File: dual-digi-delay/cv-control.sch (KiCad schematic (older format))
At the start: 44 parts, among them Q3 2N3904, Q4 2N3904, Q5 2N3904, Q6 2N3904, U5 TL074, U6 TL074

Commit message: Final revision of dual digi delay
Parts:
- added C56: 10pF, rumblesan-footprints:C_Rect_L7.0mm_W3.5mm_P5.00mm, symbol Device:C
- added D13, D14, D15, D16: 1n4148, rumblesan-footprints:Diode_THT_P7.62mm_Horizontal, symbol Device:D
- added R64, R66: 10k, rumblesan-footprints:Resistor_THT_L6.3mm_D2.5mm_P10.16mm_Horizontal, symbol Device:R
- added R65, R67: 1k, rumblesan-footprints:Resistor_THT_L6.3mm_D2.5mm_P10.16mm_Horizontal, symbol Device:R
- added R68, R69: 47k, rumblesan-footprints:Resistor_THT_L6.3mm_D2.5mm_P10.16mm_Horizontal, symbol Device:R
- R35: value 47k -> 100k
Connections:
- net DELAY1_CONTROL: now also R37.1; no longer R37.2
- net DELAY1_CV_ATTV: now also U6.3 (+), R69.1; no longer U6.5 (+)
- net DELAY2_CONTROL: now also R43.1; no longer R43.2
- net DELAY2_CV_ATTV: now also U6.12 (+), R68.1; no longer U5.3 (+)
- net DELAY2_CV_CTRL: now also U6.8, C56.1, R66.1, R68.2; no longer U5.7
- net GND: now also U5.3 (+), U6.5 (+), R65.1, R67.1; no longer U6.12 (+), U6.3 (+)
- net at R31.2, R32.2, R33.1: now also U6.9 (-), C56.2, D15.1 (K), D16.2 (A); no longer U5.6 (-)
- net at C45.2, R51.2: now also U5.14; no longer U5.8
- net at C45.1, Q3.3 (C), R50.2: now also U5.13 (-); no longer U5.9 (-)
- net at C43.2, R42.1, R44.1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: now also U5.9 (-); no longer R43.1, U5.13 (-)
- net at C43.1, R48.1: now also U5.8; no longer U5.14
- net at C41.1, R40.1, R42.2: now also U6.14; no longer U5.1
- net at C41.2, R36.1, R40.2: now also R43.2, U6.13 (-); no longer U5.2 (-)
- net at C40.2, R30.1, R34.2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: now also D13.1 (K), D14.2 (A)
- net DELAY1_CV_CTRL: now reaches C40.1, R34.1, R35.2, U6.7
- net DELAY1_CV_CTRL: now also R64.1, R69.2
- net at C46.2, R53.2: now also U5.1; no longer U6.8
- net at C46.1, Q4.3 (C), R52.2: now also U5.2 (-); no longer U6.9 (-)
- net at C44.2, R45.1, R47.2: now also R39.1, U5.6 (-); no longer U6.13 (-)
- net at C44.1, R49.1: now also U5.7; no longer U6.14
- net at C42.2, R35.1, R41.2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: now also R37.2; no longer R37.1, R39.1
- new net: D13.2 (A), D14.1 (K), R64.2, R65.2
- new net: D15.2 (A), D16.1 (K), R66.2, R67.2
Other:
- note added: "POT CW\nPIN 3"
- moved on the sheet: C36, C37, C38, C39, C40, C41, C43, C45, Q3, Q5, R29, R30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

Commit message: Finalising rev 01 of dual digi delay
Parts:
- R37, R43: value 100k -> 220k
- R42: value 47k -> 100k
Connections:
- net +VCC: no longer R39.2, R44.2
- net -VCC: now also R39.2, R44.2
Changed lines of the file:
@@
 $Descr A4 11693 8268
 encoding utf-8
-Sheet 10 10
+Sheet 9 10
 Title ""
 Date ""
@@
 AR Path="/642384B2/642A547E" Ref="R42"  Part="1"
 F 0 "R42" V 6443 5150 50  0000 C CNN
-F 1 "47k" V 6534 5150 50  0000 C CNN
+F 1 "100k" V 6534 5150 50  0000 C CNN
 F 2 "rumblesan-footprints:Resistor_THT_L6.3mm_D2.5mm_P10.16mm_Horizontal" V 6580 5150 50  0001 C CNN
 F 3 "~" H 6650 5150 50  0001 C CNN
@@
 AR Path="/642A54A8" Ref="U?"  Part="1"
 AR Path="/642384B2/642A54A8" Ref="U5"  Part="1"
-F 0 "U5" H 9000 2533 50  0000 C CNN
-F 1 "TL074" H 9000 2624 50  0000 C CNN
+F 0 "U5" H 9000 3200 50  0000 C CNN
+F 1 "TL074" H 9000 3100 50  0000 C CNN
 F 2 "rumblesan-footprints:DIP-14_W7.62mm_Socket" H 8950 3000 50  0001 C CNN
 F 3 "http://www.ti.com/lit/ds/symlink/tl071.pdf" H 9050 3100 50  0001 C CNN
@@
 AR Path="/642384B2/642A55A5" Ref="R43"  Part="1"
 F 0 "R43" V 5093 4200 50  0000 C CNN
-F 1 "100k" V 5184 4200 50  0000 C CNN
+F 1 "220k" V 5184 4200 50  0000 C CNN
 F 2 "rumblesan-footprints:Resistor_THT_L6.3mm_D2.5mm_P10.16mm_Horizontal" V 5230 4200 50  0001 C CNN
 F 3 "~" H 5300 4200 50  0001 C CNN
@@
 AR Path="/642384B2/642A55EA" Ref="R37"  Part="1"
 F 0 "R37" V 5093 1150 50  0000 C CNN
-F 1 "100k" V 5184 1150 50  0000 C CNN
+F 1 "220k" V 5184 1150 50  0000 C CNN
 F 2 "rumblesan-footprints:Resistor_THT_L6.3mm_D2.5mm_P10.16mm_Horizontal" V 5230 1150 50  0001 C CNN
 F 3 "~" H 5300 1150 50  0001 C CNN
@@
 Text Label 7250 2350 2    50   ~ 0
 GND1
-Text Label 6450 900  2    50   ~ 0
-+VCC
 Text Label 4700 3150 3    50   ~ 0
 GND1
@@
 Text Label 8800 6000 2    50   ~ 0
 GND1
-Text Label 6650 4050 2    50   ~ 0
-+VCC
 Text Label 9450 3850 2    50   ~ 0
 +VCC
@@
 	1    0    0    1
 $EndComp
+Text Label 6450 900  2    50   ~ 0
+-VCC
+Text Label 6650 4050 2    50   ~ 0
+-VCC
 $EndSCHEMATC

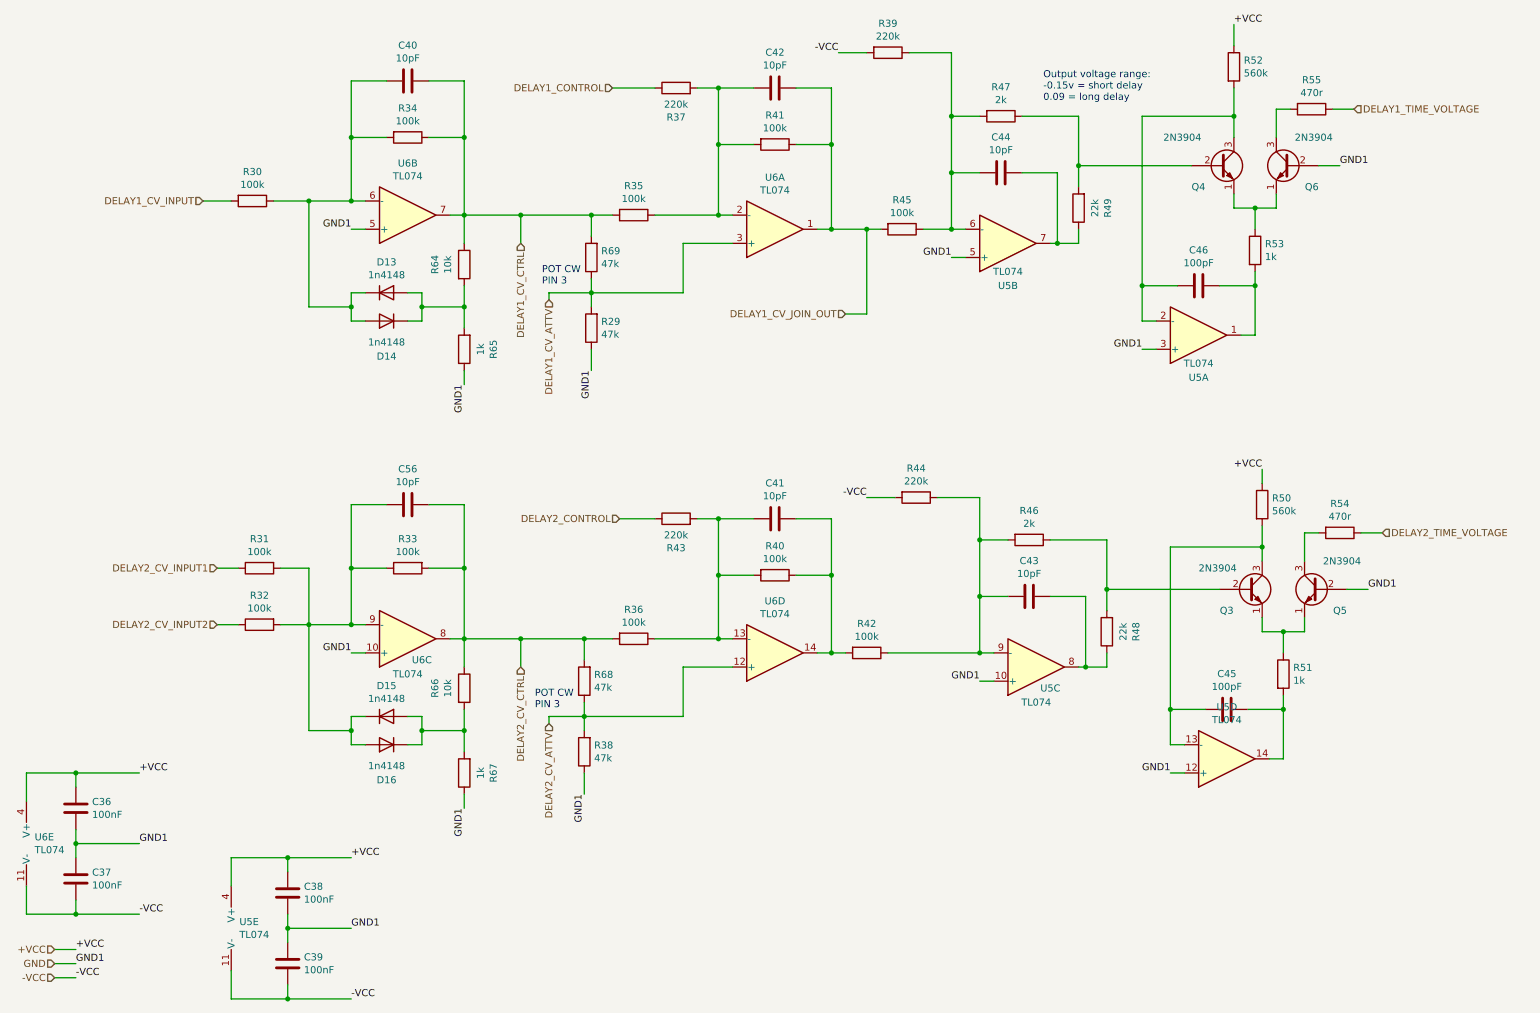
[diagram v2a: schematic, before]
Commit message: Updating digi delay to rev 2
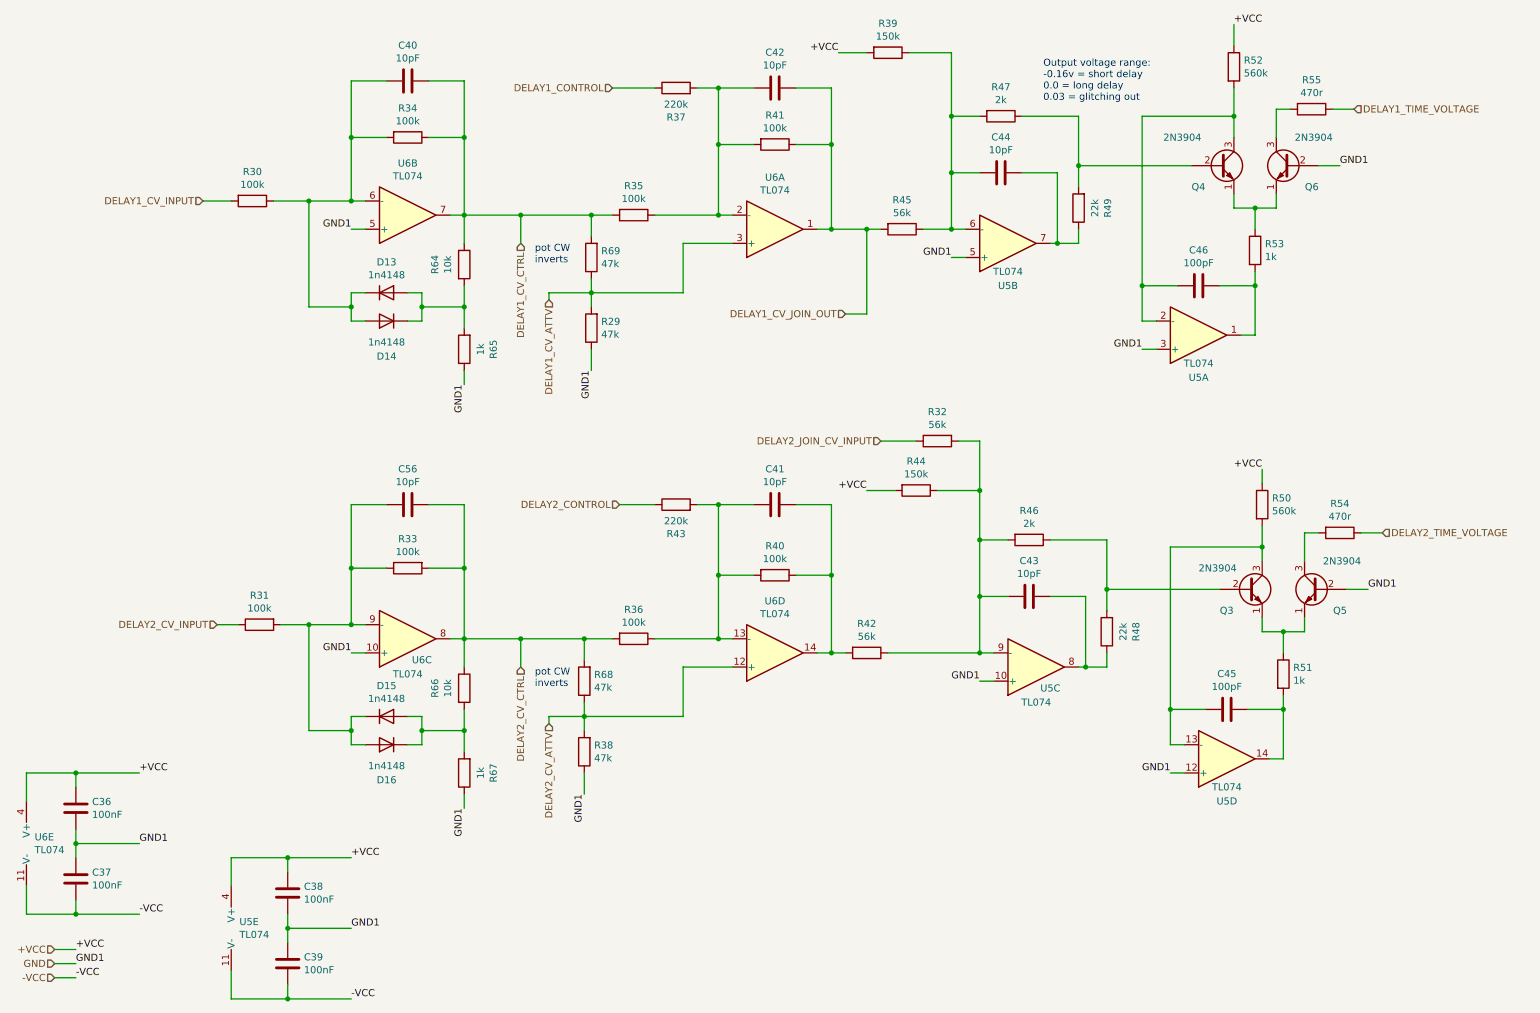
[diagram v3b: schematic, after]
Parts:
- Q3, Q4, Q5, Q6: footprint Package_TO_SOT_THT:TO-92_Inline -> Package_TO_SOT_THT:TO-92_Inline_Wide
- R32, R42, R45: value 100k -> 56k
- R39, R44: value 220k -> 150k
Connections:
- net +VCC: now also R39.2, R44.2
- net -VCC: no longer R39.2, R44.2
- net at C43.2, R42.1, R44.1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: now also R32.2
- net at C56.2, D15.1 (K), D16.2 (A)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: no longer R32.2
- net DELAY2_CV_INPUT1 renamed DELAY2_CV_INPUT
- net DELAY2_CV_INPUT2 renamed DELAY2_JOIN_CV_INPUT
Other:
- note added: "Output voltage range:\n-0.16v = short delay\n0.0 = long delay\n0.03 = glitching out"
- note added: "pot CW\ninverts"
- note removed: "Output voltage range:\n-0.15v = short delay\n0.09 = long delay"
- note removed: "POT CW\nPIN 3"
- moved on the sheet: C41, R31, R32, R43, R44
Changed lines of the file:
@@
 $Descr A4 11693 8268
 encoding utf-8
-Sheet 9 10
+Sheet 8 11
 Title ""
 Date ""
@@
 L Device:R R?
 U 1 1 642A5416
-P 7000 4050
+P 7000 4000
 AR Path="/642A5416" Ref="R?"  Part="1"
 AR Path="/642384B2/642A5416" Ref="R44"  Part="1"
-F 0 "R44" V 6793 4050 50  0000 C CNN
-F 1 "220k" V 6884 4050 50  0000 C CNN
-F 2 "rumblesan-footprints:Resistor_THT_L6.3mm_D2.5mm_P10.16mm_Horizontal" V 6930 4050 50  0001 C CNN
-F 3 "~" H 7000 4050 50  0001 C CNN
-	1    7000 4050
-	0    1    1    0
-$EndComp
-Wire Wire Line
-	7150 4050 7450 4050
-Wire Wire Line
-	6650 4050 6850 4050
+F 0 "R44" V 6793 4000 50  0000 C CNN
+F 1 "150k" V 6884 4000 50  0000 C CNN
+F 2 "rumblesan-footprints:Resistor_THT_L6.3mm_D2.5mm_P10.16mm_Horizontal" V 6930 4000 50  0001 C CNN
+F 3 "~" H 7000 4000 50  0001 C CNN
+	1    7000 4000
+	0    1    1    0
+$EndComp
+Wire Wire Line
+	7150 4000 7450 4000
+Wire Wire Line
+	6650 4000 6850 4000
 Wire Wire Line
 	7450 5150 7450 4750
@@
 	7650 4750 7450 4750
 Connection ~ 7450 4750
-Wire Wire Line
-	7450 4750 7450 4350
 Wire Wire Line
 	7950 4350 8350 4350
@@
 F 0 "Q5" H 9650 4550 50  0000 L CNN
 F 1 "2N3904" H 9550 4900 50  0000 L CNN
-F 2 "Package_TO_SOT_THT:TO-92_Inline" H 10050 4625 50  0001 L CIN
+F 2 "Package_TO_SOT_THT:TO-92_Inline_Wide" H 10050 4625 50  0001 L CIN
 F 3 "https://www.onsemi.com/pub/Collateral/2N3903-D.PDF" H 9850 4700 50  0001 L CNN
 	1    9850 4700
@@
 Connection ~ 5600 4600
 Wire Wire Line
-	5850 4200 5600 4200
+	5850 4100 5600 4100
 Connection ~ 6400 4600
 Wire Wire Line
-	6400 4200 6150 4200
-Wire Wire Line
-	6400 4600 6400 4200
+	6400 4100 6150 4100
 Wire Wire Line
 	6400 5150 6500 5150
@@
 AR Path="/642384B2/642A547E" Ref="R42"  Part="1"
 F 0 "R42" V 6443 5150 50  0000 C CNN
-F 1 "100k" V 6534 5150 50  0000 C CNN
+F 1 "56k" V 6534 5150 50  0000 C CNN
 F 2 "rumblesan-footprints:Resistor_THT_L6.3mm_D2.5mm_P10.16mm_Horizontal" V 6580 5150 50  0001 C CNN
 F 3 "~" H 6650 5150 50  0001 C CNN
@@
 L Device:C C?
 U 1 1 642A5484
-P 6000 4200
+P 6000 4100
 AR Path="/642A5484" Ref="C?"  Part="1"
 AR Path="/642384B2/642A5484" Ref="C41"  Part="1"
-F 0 "C41" V 5748 4200 50  0000 C CNN
-F 1 "10pF" V 5839 4200 50  0000 C CNN
-F 2 "rumblesan-footprints:C_Rect_L7.0mm_W3.5mm_P5.00mm" H 6038 4050 50  0001 C CNN
-F 3 "~" H 6000 4200 50  0001 C CNN
-	1    6000 4200
+F 0 "C41" V 5748 4100 50  0000 C CNN
+F 1 "10pF" V 5839 4100 50  0000 C CNN
+F 2 "rumblesan-footprints:C_Rect_L7.0mm_W3.5mm_P5.00mm" H 6038 3950 50  0001 C CNN
+F 3 "~" H 6000 4100 50  0001 C CNN
+	1    6000 4100
 	0    1    1    0
 $EndComp
@@
 F 0 "Q6" H 9450 1550 50  0000 L CNN
 F 1 "2N3904" H 9350 1900 50  0000 L CNN
-F 2 "Package_TO_SOT_THT:TO-92_Inline" H 9850 1625 50  0001 L CIN
+F 2 "Package_TO_SOT_THT:TO-92_Inline_Wide" H 9850 1625 50  0001 L CIN
 F 3 "https://www.onsemi.com/pub/Collateral/2N3903-D.PDF" H 9650 1700 50  0001 L CNN
 	1    9650 1700
@@
 F 0 "Q4" H 8950 1550 50  0000 L CNN
 F 1 "2N3904" H 8750 1900 50  0000 L CNN
-F 2 "Package_TO_SOT_THT:TO-92_Inline" H 9350 1625 50  0001 L CIN
+F 2 "Package_TO_SOT_THT:TO-92_Inline_Wide" H 9350 1625 50  0001 L CIN
 F 3 "https://www.onsemi.com/pub/Collateral/2N3903-D.PDF" H 9150 1700 50  0001 L CNN
 	1    9150 1700
@@
 AR Path="/642384B2/642A558B" Ref="R45"  Part="1"
 F 0 "R45" V 6693 2150 50  0000 C CNN
-F 1 "100k" V 6784 2150 50  0000 C CNN
+F 1 "56k" V 6784 2150 50  0000 C CNN
 F 2 "rumblesan-footprints:Resistor_THT_L6.3mm_D2.5mm_P10.16mm_Horizontal" V 6830 2150 50  0001 C CNN
 F 3 "~" H 6900 2150 50  0001 C CNN
@@
 L Device:R R?
 U 1 1 642A55A5
-P 5300 4200
+P 5300 4100
 AR Path="/642A55A5" Ref="R?"  Part="1"
 AR Path="/642384B2/642A55A5" Ref="R43"  Part="1"
-F 0 "R43" V 5093 4200 50  0000 C CNN
-F 1 "220k" V 5184 4200 50  0000 C CNN
-F 2 "rumblesan-footprints:Resistor_THT_L6.3mm_D2.5mm_P10.16mm_Horizontal" V 5230 4200 50  0001 C CNN
-F 3 "~" H 5300 4200 50  0001 C CNN
-	1    5300 4200
+F 0 "R43" V 5093 4100 50  0000 C CNN
+F 1 "220k" V 5184 4100 50  0000 C CNN
+F 2 "rumblesan-footprints:Resistor_THT_L6.3mm_D2.5mm_P10.16mm_Horizontal" V 5230 4100 50  0001 C CNN
+F 3 "~" H 5300 4100 50  0001 C CNN
+	1    5300 4100
 	0    -1   -1   0
 $EndComp
 Text Notes 7900 1250 0    50   ~ 0
-Output voltage range:\n-0.15v = short delay\n0.09 = long delay
+Output voltage range:\n-0.16v = short delay\n0.0 = long delay\n0.03 = glitching out
 Wire Wire Line
 	7050 2150 7250 2150
@@
 L Device:R R?
 U 1 1 642A55BC
-P 2350 4550
+P 2350 4950
 AR Path="/642A55BC" Ref="R?"  Part="1"
 AR Path="/642384B2/642A55BC" Ref="R31"  Part="1"
-F 0 "R31" V 2143 4550 50  0000 C CNN
-F 1 "100k" V 2234 4550 50  0000 C CNN
-F 2 "rumblesan-footprints:Resistor_THT_L6.3mm_D2.5mm_P10.16mm_Horizontal" V 2280 4550 50  0001 C CNN
-F 3 "~" H 2350 4550 50  0001 C CNN
-	1    2350 4550
-	0    -1   1    0
-$EndComp
-Wire Wire Line
-	2050 4550 2200 4550
-Wire Wire Line
-	3000 4950 3000 4550
-Wire Wire Line
-	3000 4550 3250 4550
-Wire Wire Line
-	3000 4950 3100 4950
-Wire Wire Line
-	3700 5050 3800 5050
-Wire Wire Line
-	3550 4550 3800 4550
-Wire Wire Line
-	3800 4550 3800 5050
-Connection ~ 3800 5050
-$Comp
-L Device:R R?
-U 1 1 642A55CC
-P 2350 4950
-AR Path="/642A55CC" Ref="R?"  Part="1"
-AR Path="/642384B2/642A55CC" Ref="R32"  Part="1"
-F 0 "R32" V 2143 4950 50  0000 C CNN
+F 0 "R31" V 2143 4950 50  0000 C CNN
 F 1 "100k" V 2234 4950 50  0000 C CNN
 F 2 "rumblesan-footprints:Resistor_THT_L6.3mm_D2.5mm_P10.16mm_Horizontal" V 2280 4950 50  0001 C CNN
@@
 	0    -1   1    0
 $EndComp
+Wire Wire Line
+	2050 4950 2200 4950
+Wire Wire Line
+	3000 4950 3000 4550
+Wire Wire Line
+	3000 4550 3250 4550
+Wire Wire Line
+	3000 4950 3100 4950
+Wire Wire Line
+	3700 5050 3800 5050
+Wire Wire Line
+	3550 4550 3800 4550
+Wire Wire Line
+	3800 4550 3800 5050
+Connection ~ 3800 5050
 $Comp
 L Device:R R?
@@
 AR Path="/642384B2/642A55DA" Ref="R39"  Part="1"
 F 0 "R39" V 6593 900 50  0000 C CNN
-F 1 "220k" V 6684 900 50  0000 C CNN
+F 1 "150k" V 6684 900 50  0000 C CNN
 F 2 "rumblesan-footprints:Resistor_THT_L6.3mm_D2.5mm_P10.16mm_Horizontal" V 6730 900 50  0001 C CNN
 F 3 "~" H 6800 900 50  0001 C CNN
@@
 	4650 6000 4650 6150
 Wire Wire Line
-	2200 4950 2050 4950
-Wire Wire Line
 	8600 2550 8600 1350
 Wire Wire Line
@@
 F 0 "Q3" H 9150 4550 50  0000 L CNN
 F 1 "2N3904" H 9000 4850 50  0000 L CNN
-F 2 "Package_TO_SOT_THT:TO-92_Inline" H 9550 4625 50  0001 L CIN
+F 2 "Package_TO_SOT_THT:TO-92_Inline_Wide" H 9550 4625 50  0001 L CIN
 F 3 "https://www.onsemi.com/pub/Collateral/2N3903-D.PDF" H 9350 4700 50  0001 L CNN
 	1    9350 4700
@@
 AR Path="/642A55AE" Ref="U?"  Part="4"
 AR Path="/642384B2/642A55AE" Ref="U5"  Part="4"
-F 0 "U5" H 9200 5533 50  0000 C CNN
-F 1 "TL074" H 9200 5624 50  0000 C CNN
+F 0 "U5" H 9200 6200 50  0000 C CNN
+F 1 "TL074" H 9200 6100 50  0000 C CNN
 F 2 "rumblesan-footprints:DIP-14_W7.62mm_Socket" H 9150 6000 50  0001 C CNN
 F 3 "http://www.ti.com/lit/ds/symlink/tl071.pdf" H 9250 6100 50  0001 C CNN
@@
 Text Label 4650 6150 3    50   ~ 0
 GND1
-Text HLabel 4900 4200 0    50   Input ~ 0
+Text HLabel 4900 4100 0    50   Input ~ 0
 DELAY2_CONTROL
 Text Label 7450 5350 2    50   ~ 0
@@
 	1    0    0    -1
 $EndComp
+Text HLabel 6750 3650 0    50   Input ~ 0
+DELAY2_JOIN_CV_INPUT
 Text HLabel 2050 4950 0    50   Input ~ 0
-DELAY2_CV_INPUT2
-Text HLabel 2050 4550 0    50   Input ~ 0
-DELAY2_CV_INPUT1
+DELAY2_CV_INPUT
+Wire Wire Line
+	7300 3650 7450 3650
+Connection ~ 2700 4950
 Wire Wire Line
 	2500 4950 2700 4950
-Connection ~ 2700 4950
-Wire Wire Line
-	2700 4550 2700 4950
-Wire Wire Line
-	2500 4550 2700 4550
 Wire Wire Line
 	3800 5050 4200 5050
@@
 Connection ~ 5600 5050
 Wire Wire Line
-	4900 4200 5150 4200
-Wire Wire Line
-	5450 4200 5600 4200
-Wire Wire Line
-	7450 4050 7450 4350
+	4900 4100 5150 4100
+Wire Wire Line
+	5450 4100 5600 4100
 Wire Wire Line
 	6800 5150 7450 5150
@@
 Wire Wire Line
 	7250 900  7250 1350
-Connection ~ 7450 4350
-Connection ~ 5600 4200
-Wire Wire Line
-	5600 4200 5600 4600
-Text Notes 4350 2550 0    50   ~ 0
-POT CW\nPIN 3
-Text Notes 4300 5550 0    50   ~ 0
-POT CW\nPIN 3
 $Comp
 L Device:C C?
@@
 	1    0    0    1
 $EndComp
+Wire Wire Line
+	6750 3650 7000 3650
+Wire Wire Line
+	6400 4100 6400 4600
 Text Label 6450 900  2    50   ~ 0
--VCC
-Text Label 6650 4050 2    50   ~ 0
--VCC
++VCC
+Text Label 6650 4000 2    50   ~ 0
++VCC
+$Comp
+L Device:R R?
+U 1 1 642A55CC
+P 7150 3650
+AR Path="/642A55CC" Ref="R?"  Part="1"
+AR Path="/642384B2/642A55CC" Ref="R32"  Part="1"
+F 0 "R32" V 6943 3650 50  0000 C CNN
+F 1 "56k" V 7034 3650 50  0000 C CNN
+F 2 "rumblesan-footprints:Resistor_THT_L6.3mm_D2.5mm_P10.16mm_Horizontal" V 7080 3650 50  0001 C CNN
+F 3 "~" H 7150 3650 50  0001 C CNN
+	1    7150 3650
+	0    -1   1    0
+$EndComp
+Text Notes 4300 2400 0    50   ~ 0
+pot CW\ninverts
+Text Notes 4300 5400 0    50   ~ 0
+pot CW\ninverts
+Wire Wire Line
+	7450 3650 7450 4000
+Connection ~ 7450 4000
+Wire Wire Line
+	7450 4000 7450 4350
+Connection ~ 7450 4350
+Wire Wire Line
+	7450 4350 7450 4750
+Connection ~ 5600 4100
+Wire Wire Line
+	5600 4100 5600 4600
 $EndSCHEMATC
